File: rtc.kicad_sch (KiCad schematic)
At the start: 8 parts, among them U1501 PCF85063ATL, Y1501 32.768kHz 7pF

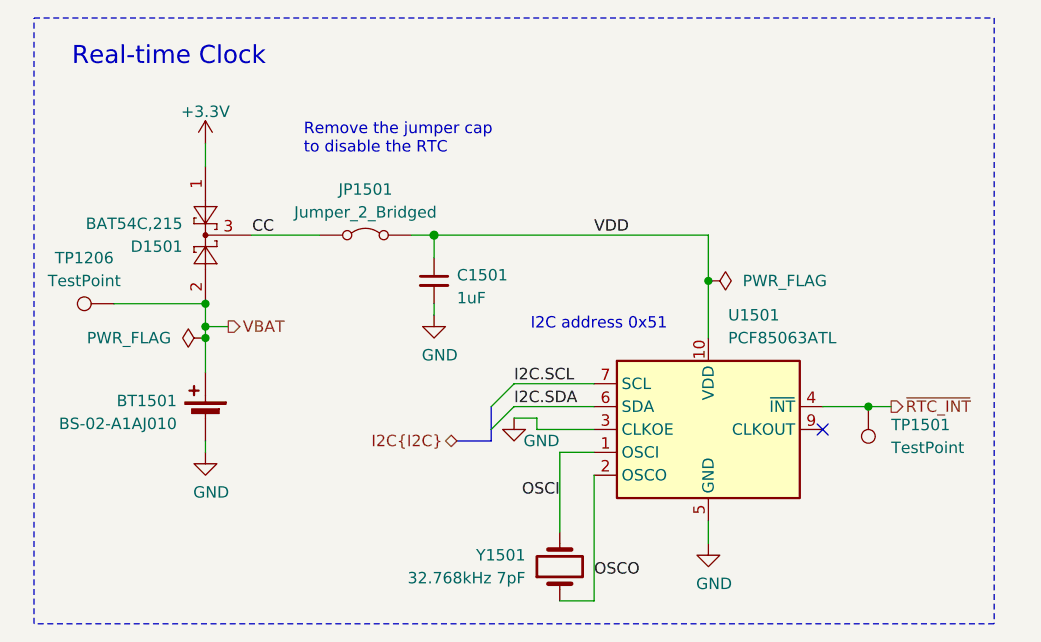
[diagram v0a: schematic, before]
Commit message: Finish transitioning to RP2040
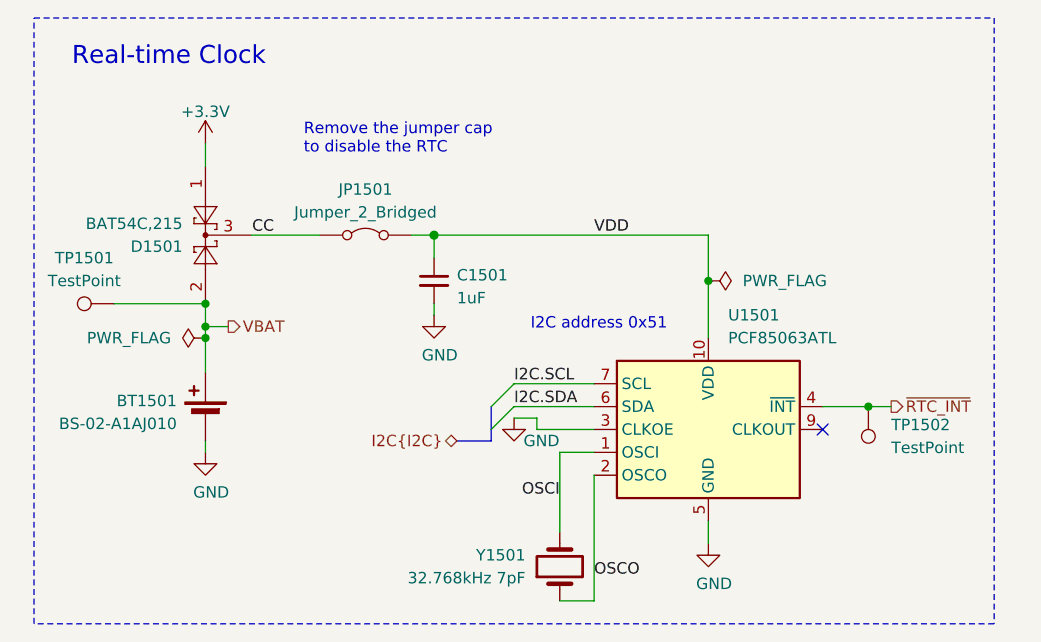
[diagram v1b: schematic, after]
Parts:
- renumbered TP1206 to TP1501, TP1501 to TP1502
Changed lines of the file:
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@@
 		(on_board yes)
 		(dnp no)
-		(property "Reference" "TP1501"
+		(property "Reference" "TP1502"
 			(at 187.96 103.6319 0)
 			(effects
@@
 			(project "HALPI2"
 				(path "/abc482bd-3f17-4d35-80db-1da3dcdb5c27/850df4bf-e40a-4082-adc2-76804638b949/e502b11a-b887-47b5-9ff1-f210171ce142"
-					(reference "TP1501")
+					(reference "TP1502")
 					(unit 1)
 				)
@@
 		(dnp no)
 		(fields_autoplaced yes)
-		(property "Reference" "TP1206"
+		(property "Reference" "TP1501"
 			(at 98.298 85.09 90)
 			(effects
@@
 			(project "HALPI2"
 				(path "/abc482bd-3f17-4d35-80db-1da3dcdb5c27/850df4bf-e40a-4082-adc2-76804638b949/e502b11a-b887-47b5-9ff1-f210171ce142"
-					(reference "TP1206")
-					(unit 1)
-				)
+					(reference "TP1501")
+					(unit 1)
+				)

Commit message: Apply part PCBA position corrections
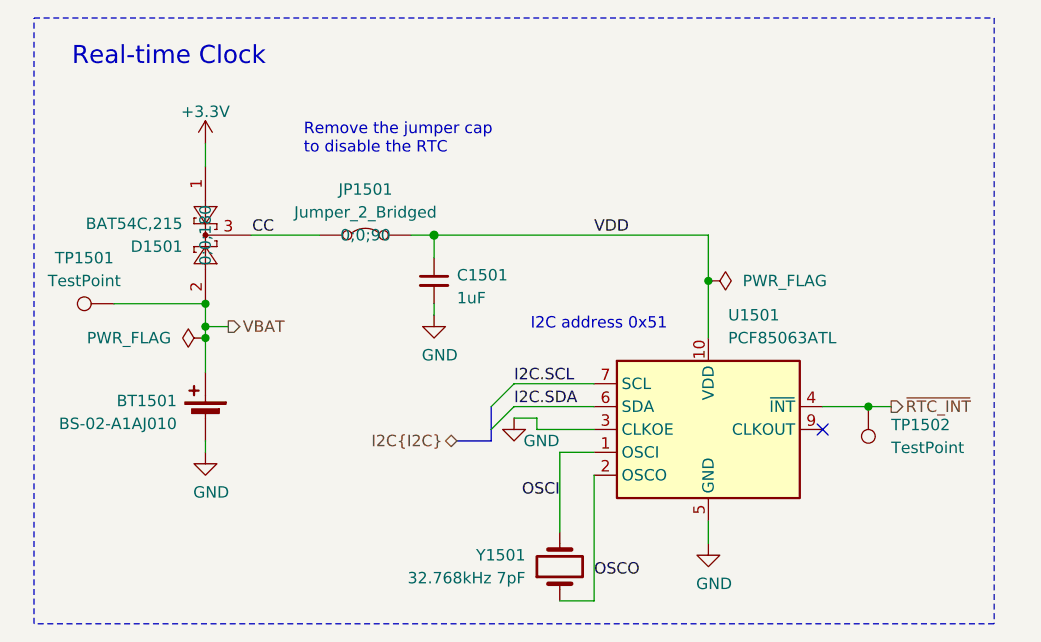
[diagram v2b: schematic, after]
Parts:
- D1501: JLCPCB_CORRECTION (none) -> 0;0;180
- JP1501: JLCPCB_CORRECTION (none) -> 0;0;90
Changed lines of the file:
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@@
+			)
+		)
+		(property "JLCPCB_CORRECTION" "0;0;180"
+			(at 111.76 82.55 0)
+			(effects
+				(font
+					(size 1.27 1.27)
+				)
 			)
 		)
@@
 			(at 129.54 82.55 0)
 			(effects
+				(font
+					(size 1.27 1.27)
+				)
+			)
+		)
+		(property "JLCPCB_CORRECTION" "0;0;90"
+			(at 129.54 82.55 0)
+			(effects
